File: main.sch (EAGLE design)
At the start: 79 parts, among them Q1 5.8A/30V/35mΩ, Q2 5.8A/30V/35mΩ, Q3 2.5A/30V/105mΩ, U2 SN65HVD32_D_8

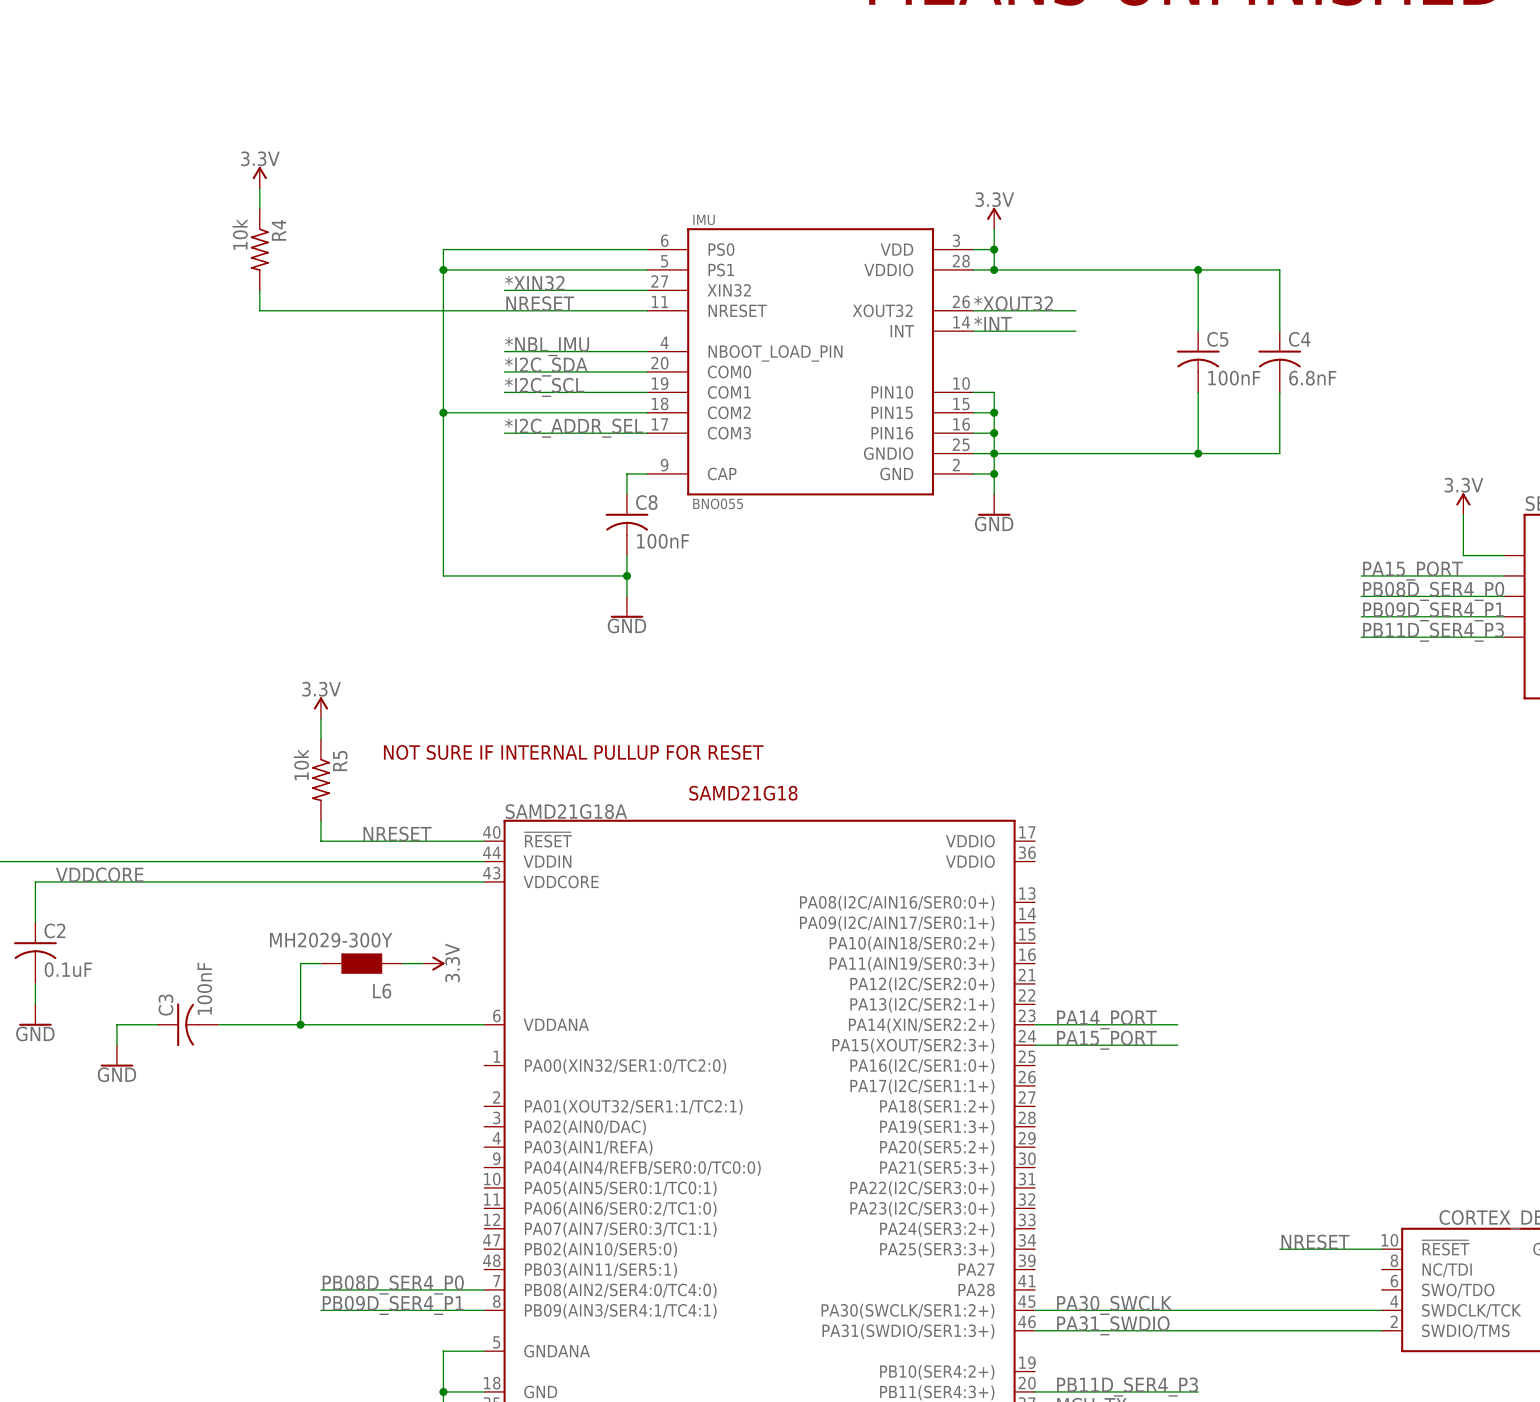
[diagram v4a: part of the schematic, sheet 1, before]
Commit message: Finished board Layout
First attempt at a board layout for the schematic, most likley not final.
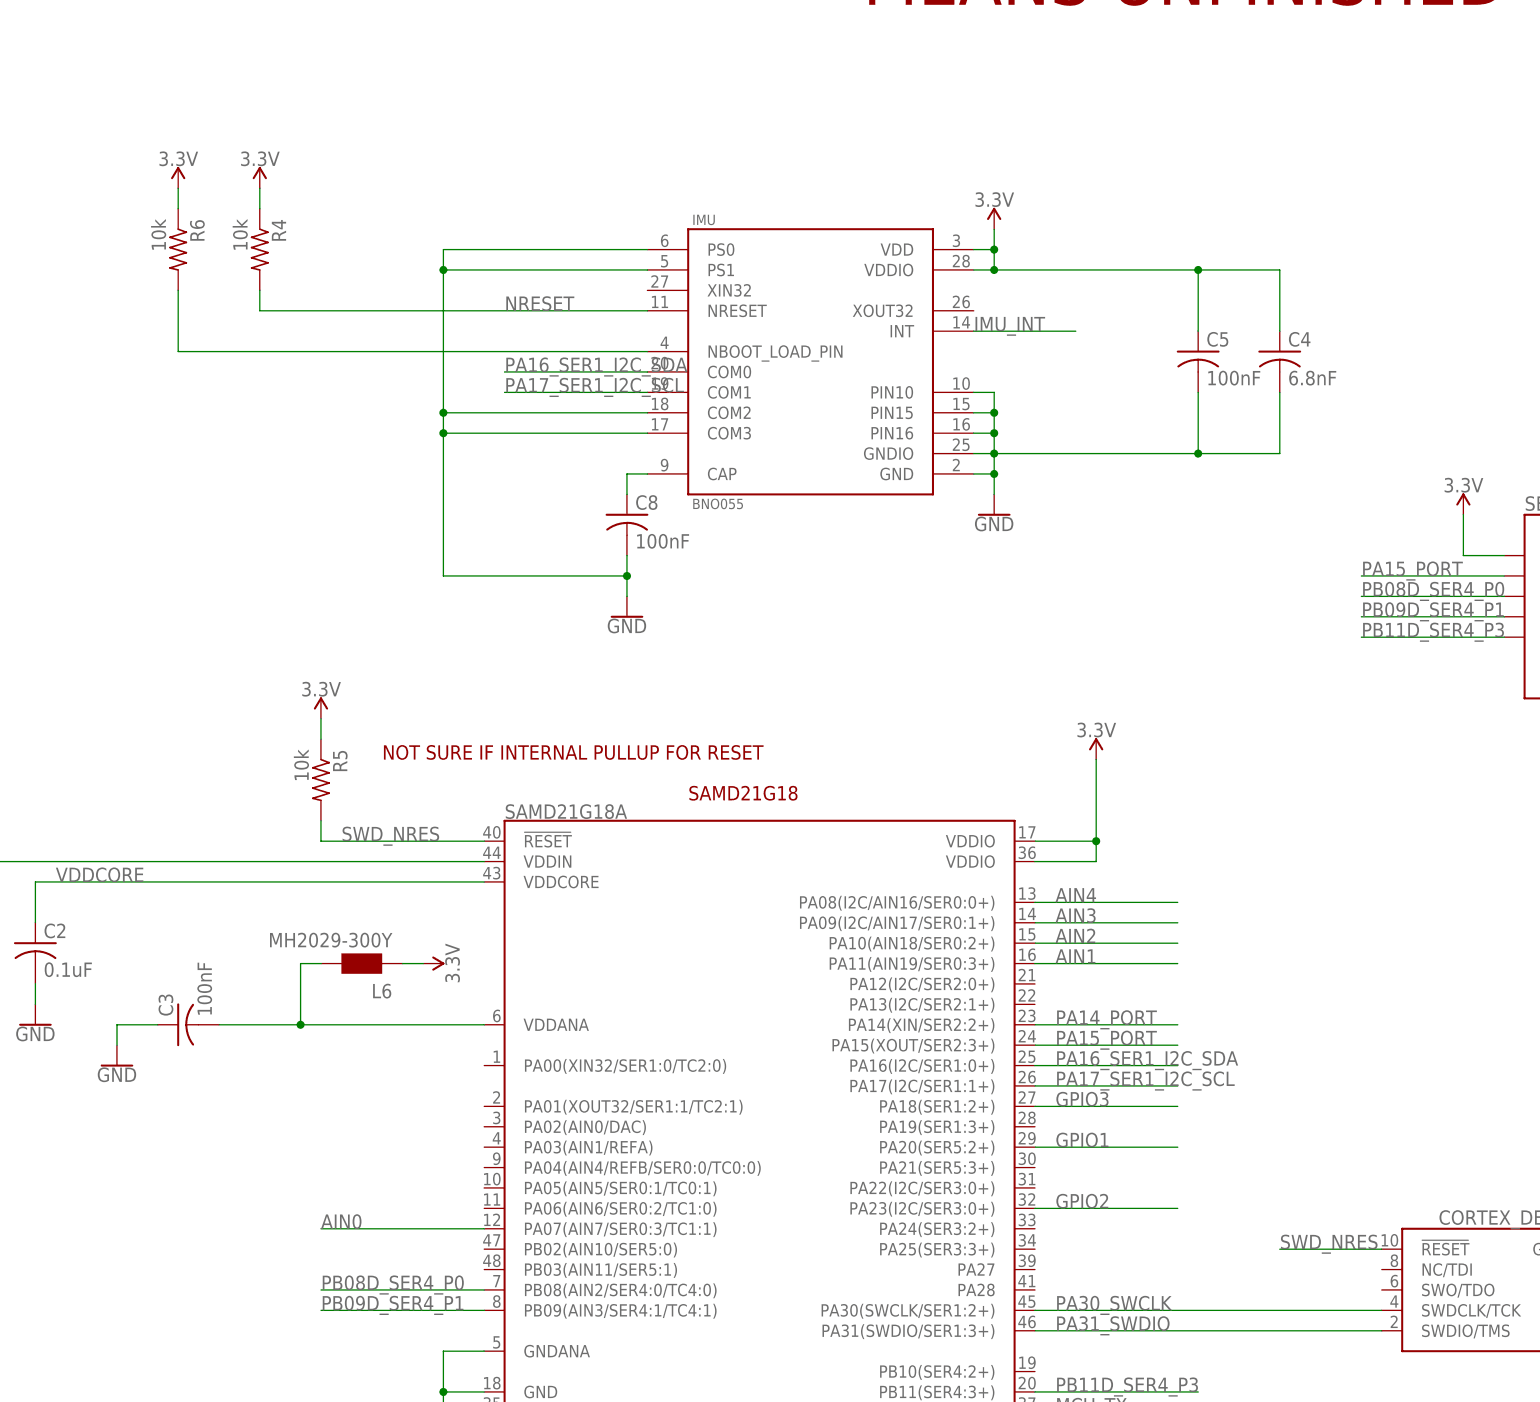
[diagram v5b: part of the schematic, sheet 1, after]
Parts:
- added R6: 10k, resistor:R-US_R0603
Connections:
- net *INT renamed IMU_INT
- removed net *I2C_ADDR_SEL: IMU.COM3
- removed net *I2C_SCL: IMU.COM1
- removed net *I2C_SDA: IMU.COM0
- removed net *NBL_IMU: IMU.NBOOT_LOAD_PIN
- removed net *XIN32: IMU.XIN32
- removed net *XOUT32: IMU.XOUT32
- new net N$18: IMU.NBOOT_LOAD_PIN, R6.2
- new net PA16_SER1_I2C_SDA: IMU.COM0, SAMD21G18A.PA16(I2C/SER1:0+)
- new net PA17_SER1_I2C_SCL: IMU.COM1, SAMD21G18A.PA17(I2C/SER1:1+)
- new net SWD_NRES: R5.2, SAMD21G18A.!RESET!, SWD.!RESET
- net 3.3V: now also R6.1, SAMD21G18A.VDDIO@17, SAMD21G18A.VDDIO@36
- net AIN0: now also SAMD21G18A.PA07(AIN7/SER0:3/TC1:1)
- net AIN1: now also SAMD21G18A.PA11(AIN19/SER0:3+)
- net AIN2: now also SAMD21G18A.PA10(AIN18/SER0:2+)
- net AIN3: now also SAMD21G18A.PA09(I2C/AIN17/SER0:1+)
- net AIN4: now also SAMD21G18A.PA08(I2C/AIN16/SER0:0+)
- net GND: now also IMU.COM3
- net GPIO1: now also SAMD21G18A.PA20(SER5:2+)
- net GPIO2: now also SAMD21G18A.PA23(I2C/SER3:0+)
- net GPIO3: now also SAMD21G18A.PA18(SER1:2+)
- net NRESET: no longer R5.2, SAMD21G18A.!RESET!, SWD.!RESET

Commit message: Reworked Layout, added thermocouple ics
Second attempt at a board layout, more balanced spacing.
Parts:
- removed S1: (no value), switch:M251
- added C10, C24, C27, C28, C29, C32: 100nF, resistor:C-USC0603
- added C25, C26, C30, C31: 10nF, resistor:C-USC0603
- added R22, R36, R37: 100, resistor:R-US_R0603
- added S2: (no value), SparkFun-Switches:SWITCH-SPDT-SMD-AYZ0202
- added TC0, TC1: MAX31856, microbuilder:MAX31856
- added TCIN0, TCIN1: (no value), pinhead:PINHD-1X2
- R33: value 0 -> 100
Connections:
- removed net PC_CELL: POWER_CONTROLLER.CELL, R33.2
- new net N$21: C10.1, C26.2, R33.2, TC0.T-
- new net N$22: C10.2, C25.1, R22.2, TC0.T+
- new net N$23: R33.1, TC0.BIAS, TCIN0.2
- new net N$24: R22.1, TCIN0.1
- new net N$25: C28.1, C31.2, R37.2, TC1.T-
- new net N$26: C28.2, C30.1, R36.2, TC1.T+
- new net N$27: R37.1, TC1.BIAS, TCIN1.2
- new net N$28: R36.1, TCIN1.1
- new net TC0_CS: TC0.!CS
- new net TC0_DRDY: TC0.!DRDY
- new net TC0_FAULT: TC0.!FAULT
- new net TC1_CS: TC1.!CS
- new net TC1_DRDY: TC1.!DRDY
- new net TC1_FAULT: TC1.!FAULT
- net 3.3V: now also C24.1, C27.1, C29.1, C32.1, TC0.AVDD, TC0.DVDD, TC1.AVDD, TC1.DVDD
- net AIN0: no longer SAMD21G18A.PA07(AIN7/SER0:3/TC1:1)
- net AIN1: no longer SAMD21G18A.PA11(AIN19/SER0:3+)
- net AIN2: no longer SAMD21G18A.PA10(AIN18/SER0:2+)
- net AIN3: no longer SAMD21G18A.PA09(I2C/AIN17/SER0:1+)
- net AIN4: no longer SAMD21G18A.PA08(I2C/AIN16/SER0:0+)
- net GND: now also C24.2, C25.2, C26.1, C27.2, C29.2, C30.2, C31.1, C32.2, TC0.AGND, TC0.DGND, TC1.AGND, TC1.DGND
- net GPIO1: no longer SAMD21G18A.PA20(SER5:2+)
- net GPIO2: no longer SAMD21G18A.PA23(I2C/SER3:0+)
- net GPIO3: no longer SAMD21G18A.PA18(SER1:2+)
- net PB08D_SER4_P0: now also TC0.SDI, TC1.SDI
- net PB09D_SER4_P1: now also TC0.SCK, TC1.SCK
- net PB11D_SER4_P3: now also TC0.SDO, TC1.SDO
- net PC_PVCC: now also S2.P; no longer S1.P
- net PC_VREF: now also POWER_CONTROLLER.CELL; no longer R33.1
- net VSYS: now also S2.O; no longer S1.S

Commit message: Some fixes, layout additions
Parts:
- added R38, R39: 1k, resistor:R-US_R0603
- added R40: 10k, resistor:R-US_R0603
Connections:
- net 3.3V: now also R38.1, R39.1, R40.2
- net AIN0: now also SAMD21G18A.PA11(AIN19/SER0:3+)
- net AIN1: now also SAMD21G18A.PA10(AIN18/SER0:2+)
- net AIN2: now also SAMD21G18A.PA09(I2C/AIN17/SER0:1+)
- net AIN3: now also SAMD21G18A.PA08(I2C/AIN16/SER0:0+)
- net AIN4: now also SAMD21G18A.PA07(AIN7/SER0:3/TC1:1)
- net GND: now also SER4.CD2
- net PA14_PORT: now also R40.1; no longer SER4.CD2
- net PA16_SER1_I2C_SDA: now also R38.2
- net PA17_SER1_I2C_SCL: now also R39.2
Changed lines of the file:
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@@
 <part name="C32" library="resistor" library_urn="urn:adsk.eagle:library:348" deviceset="C-US" device="C0603" package3d_urn="urn:adsk.eagle:package:26138/1" value="100nF"/>
 <part name="SUPPLY17" library="SparkFun-PowerSymbols" deviceset="3.3V" device=""/>
+<part name="R38" library="resistor" library_urn="urn:adsk.eagle:library:348" deviceset="R-US_" device="R0603" package3d_urn="urn:adsk.eagle:package:26057/1" value="1k"/>
+<part name="R39" library="resistor" library_urn="urn:adsk.eagle:library:348" deviceset="R-US_" device="R0603" package3d_urn="urn:adsk.eagle:package:26057/1" value="1k"/>
+<part name="SUPPLY18" library="SparkFun-PowerSymbols" deviceset="3.3V" device=""/>
+<part name="GND49" library="SparkFun-PowerSymbols" deviceset="GND" device=""/>
+<part name="R40" library="resistor" library_urn="urn:adsk.eagle:library:348" deviceset="R-US_" device="R0603" package3d_urn="urn:adsk.eagle:package:26057/1" value="10k"/>
+<part name="SUPPLY19" library="SparkFun-PowerSymbols" deviceset="3.3V" device=""/>
 </parts>
 <sheets>
@@
 <instance part="C32" gate="G$1" x="551.18" y="203.2"/>
 <instance part="SUPPLY17" gate="G$1" x="551.18" y="210.82"/>
+<instance part="R38" gate="G$1" x="137.16" y="215.9" rot="R270"/>
+<instance part="R39" gate="G$1" x="127" y="215.9" rot="R270"/>
+<instance part="SUPPLY18" gate="G$1" x="132.08" y="226.06"/>
+<instance part="GND49" gate="1" x="304.8" y="147.32"/>
+<instance part="R40" gate="G$1" x="304.8" y="165.1" rot="R90"/>
+<instance part="SUPPLY19" gate="G$1" x="304.8" y="172.72"/>
 </instances>
 <busses>
@@
 <label x="403.86" y="83.82" size="1.778" layer="95"/>
 </segment>
+<segment>
+<pinref part="SAMD21G18A" gate="G$1" pin="PA08(I2C/AIN16/SER0:0+)"/>
+<wire x1="203.2" y1="124.46" x2="218.44" y2="124.46" width="0.1524" layer="91"/>
+<label x="205.74" y="124.46" size="1.778" layer="95"/>
+</segment>
 </net>
 <net name="AIN4" class="0">
@@
 <label x="426.72" y="83.82" size="1.778" layer="95"/>
 </segment>
+<segment>
+<pinref part="SAMD21G18A" gate="G$1" pin="PA07(AIN7/SER0:3/TC1:1)"/>
+<wire x1="134.62" y1="83.82" x2="114.3" y2="83.82" width="0.1524" layer="91"/>
+<label x="114.3" y="83.82" size="1.778" layer="95"/>
+</segment>
 </net>
 <net name="AIN2" class="0">
@@
 <junction x="378.46" y="83.82"/>
 <label x="381" y="83.82" size="1.778" layer="95"/>
+</segment>
+<segment>
+<pinref part="SAMD21G18A" gate="G$1" pin="PA09(I2C/AIN17/SER0:1+)"/>
+<wire x1="203.2" y1="121.92" x2="218.44" y2="121.92" width="0.1524" layer="91"/>
+<label x="205.74" y="121.92" size="1.778" layer="95"/>
 </segment>
 </net>
@@
 <wire x1="551.18" y1="137.16" x2="551.18" y2="139.7" width="0.1524" layer="91"/>
 <junction x="551.18" y="139.7"/>
+</segment>
+<segment>
+<pinref part="R39" gate="G$1" pin="1"/>
+<wire x1="127" y1="220.98" x2="127" y2="223.52" width="0.1524" layer="91"/>
+<wire x1="127" y1="223.52" x2="132.08" y2="223.52" width="0.1524" layer="91"/>
+<pinref part="R38" gate="G$1" pin="1"/>
+<wire x1="132.08" y1="223.52" x2="137.16" y2="223.52" width="0.1524" layer="91"/>
+<wire x1="137.16" y1="223.52" x2="137.16" y2="220.98" width="0.1524" layer="91"/>
+<wire x1="132.08" y1="223.52" x2="132.08" y2="226.06" width="0.1524" layer="91"/>
+<junction x="132.08" y="223.52"/>
+<pinref part="SUPPLY18" gate="G$1" pin="3.3V"/>
+</segment>
+<segment>
+<pinref part="SUPPLY19" gate="G$1" pin="3.3V"/>
+<pinref part="R40" gate="G$1" pin="2"/>
+<wire x1="304.8" y1="172.72" x2="304.8" y2="170.18" width="0.1524" layer="91"/>
 </segment>
 </net>
@@
 <wire x1="551.18" y1="195.58" x2="551.18" y2="198.12" width="0.1524" layer="91"/>
 </segment>
+<segment>
+<wire x1="304.8" y1="152.4" x2="304.8" y2="149.86" width="0.1524" layer="91"/>
+<pinref part="GND49" gate="1" pin="GND"/>
+<pinref part="SER4" gate="1" pin="CD2"/>
+<wire x1="294.64" y1="152.4" x2="304.8" y2="152.4" width="0.1524" layer="91"/>
+</segment>
 </net>
 <net name="VDDCORE" class="0">
@@
 <label x="335.28" y="83.82" size="1.778" layer="95"/>
 </segment>
+<segment>
+<pinref part="SAMD21G18A" gate="G$1" pin="PA11(AIN19/SER0:3+)"/>
+<wire x1="203.2" y1="116.84" x2="218.44" y2="116.84" width="0.1524" layer="91"/>
+<label x="205.74" y="116.84" size="1.778" layer="95"/>
+</segment>
 </net>
 <net name="AIN1" class="0">
@@
 <junction x="355.6" y="83.82"/>
 <label x="358.14" y="83.82" size="1.778" layer="95"/>
+</segment>
+<segment>
+<pinref part="SAMD21G18A" gate="G$1" pin="PA10(AIN18/SER0:2+)"/>
+<wire x1="203.2" y1="119.38" x2="218.44" y2="119.38" width="0.1524" layer="91"/>
+<label x="205.74" y="119.38" size="1.778" layer="95"/>
 </segment>
 </net>
@@
 <net name="PA14_PORT" class="0">
 <segment>
-<pinref part="SER4" gate="1" pin="CD2"/>
-<wire x1="294.64" y1="152.4" x2="297.18" y2="152.4" width="0.1524" layer="91"/>
+<label x="294.64" y="157.48" size="1.778" layer="95"/>
+<pinref part="R40" gate="G$1" pin="1"/>
+<wire x1="304.8" y1="160.02" x2="304.8" y2="157.48" width="0.1524" layer="91"/>
 <pinref part="SER4" gate="1" pin="CD1"/>
-<wire x1="297.18" y1="152.4" x2="297.18" y2="154.94" width="0.1524" layer="91"/>
-<wire x1="297.18" y1="154.94" x2="297.18" y2="157.48" width="0.1524" layer="91"/>
-<wire x1="297.18" y1="157.48" x2="294.64" y2="157.48" width="0.1524" layer="91"/>
-<wire x1="297.18" y1="154.94" x2="314.96" y2="154.94" width="0.1524" layer="91"/>
-<junction x="297.18" y="154.94"/>
-<label x="302.26" y="154.94" size="1.778" layer="95"/>
+<wire x1="304.8" y1="157.48" x2="294.64" y2="157.48" width="0.1524" layer="91"/>
 </segment>
 <segment>
@@
 <wire x1="154.94" y1="190.5" x2="137.16" y2="190.5" width="0.1524" layer="91"/>
 <label x="137.16" y="190.5" size="1.778" layer="95"/>
+<wire x1="137.16" y1="190.5" x2="137.16" y2="210.82" width="0.1524" layer="91"/>
+<pinref part="R38" gate="G$1" pin="2"/>
 </segment>
 </net>
@@
 <segment>
 <pinref part="IMU" gate="G$1" pin="COM1"/>
-<wire x1="154.94" y1="187.96" x2="137.16" y2="187.96" width="0.1524" layer="91"/>
 <label x="137.16" y="187.96" size="1.778" layer="95"/>
-</segment>
-</net>
+<wire x1="154.94" y1="187.96" x2="127" y2="187.96" width="0.1524" layer="91"/>
+<wire x1="127" y1="187.96" x2="127" y2="210.82" width="0.1524" layer="91"/>
+<pinref part="R39" gate="G$1" pin="2"/>
+</segment>
+</net>

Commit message: Finished 2nd layout
Still needs a few error corrections and status leds where possible.
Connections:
- removed net PA14_PORT: R40.1, SAMD21G18A.PA14(XIN/SER2:2+), SER4.CD1
- removed net PA15_PORT: SAMD21G18A.PA15(XOUT/SER2:3+), SER4.!CS
- new net SD_CD: R40.1, SAMD21G18A.PA03(AIN1/REFA), SER4.CD1
- new net SD_CS: SAMD21G18A.PA00(XIN32/SER1:0/TC2:0), SER4.!CS
- net GPIO1: now also SAMD21G18A.PA15(XOUT/SER2:3+)
- net GPIO2: now also SAMD21G18A.PA13(I2C/SER2:1+)
- net GPIO3: now also SAMD21G18A.PB10(SER4:2+)
- net TC0_CS: now also SAMD21G18A.PB02(AIN10/SER5:0)
- net TC0_DRDY: now also SAMD21G18A.PB03(AIN11/SER5:1)
- net TC0_FAULT: now also SAMD21G18A.PA28
- net TC1_CS: now also SAMD21G18A.PA01(XOUT32/SER1:1/TC2:1)
- net TC1_DRDY: now also SAMD21G18A.PA24(SER3:2+)
- net TC1_FAULT: now also SAMD21G18A.PA27
